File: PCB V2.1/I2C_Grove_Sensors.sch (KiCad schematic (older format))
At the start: 0 parts

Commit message: SunLeaf Alpha 0.2 and KiCAD Port
SunLeaf rev 2 called Alhpa 0.2 or 0.2a is the main component of this
commit. The entire hardware project has been ported to KiCAD libaries
and all. 0.2a features a revised formfactor, better ESP module, and many
fixes over the original. This version will also be capable of OTA
updates.
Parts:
- added C27, C28, C29, C30, C31: CL05B104JP5NNNC, PCB_Footprints:C0402, symbol CL05B104JP5NNNC
- added D6, D7, D8, D9: PESD3V3L2BT,215, PCB_Footprints:BAT20JFILM, symbol PESD3V3L2BT,215
- added J10, J11, J12, J9: S4B-PH-SM4-TB(LF)(SN), PCB_Footprints:S4B-PH-SM4-TB(LF)(SN), symbol S4B-PH-SM4-TB(LF)(SN)
- added R27, R28, R29, R30, R31, R32, R33, R34: RC1005F472CS, PCB_Footprints:R0402, symbol RC1005F472CS
- added U5: PCA9518DBQR, PCB_Footprints:PCA9518DBQR, symbol PCA9518DBQR
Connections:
- net labels added: +3.3V, GND
- wire segments 0 -> 46
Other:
- note added: "I2C Grove Sensors"

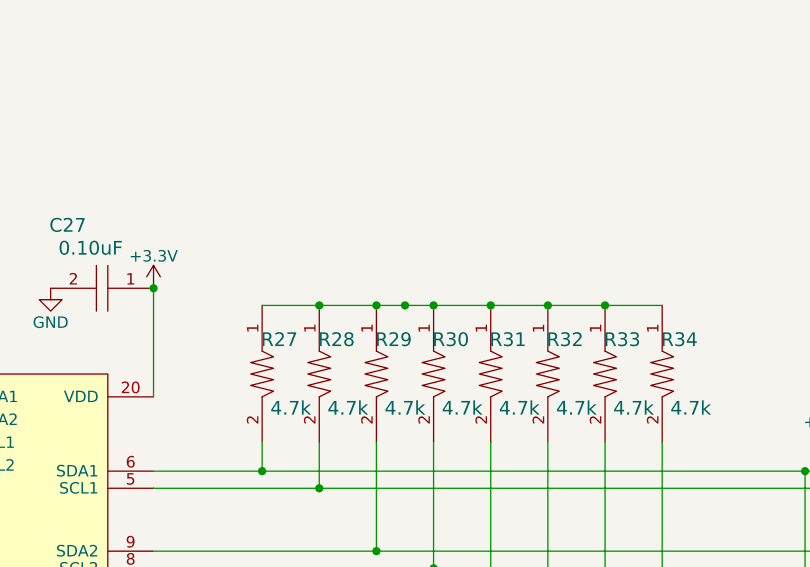
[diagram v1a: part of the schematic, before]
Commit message: Update
Updating KiCAD to the latest to get rounded corner pad support, filing
this commit as a backup of the project before update.
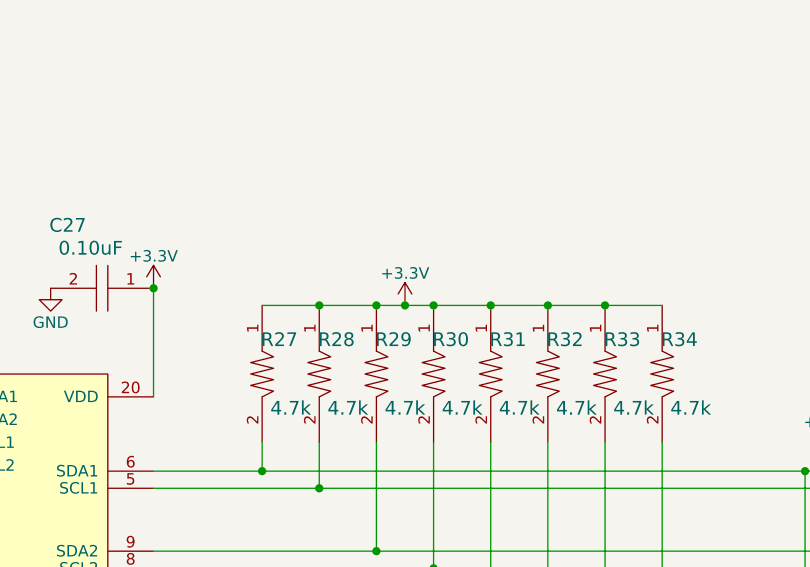
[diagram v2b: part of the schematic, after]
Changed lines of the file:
@@
 $EndComp
 $Comp
-L +3.3V #PWR053
+L +3.3V #PWR55
 U 1 1 57D9F38F
 P 2425 3000
-F 0 "#PWR053" H 2425 2850 50  0001 C CNN
+F 0 "#PWR55" H 2425 2850 50  0001 C CNN
 F 1 "+3.3V" H 2425 3140 50  0000 C CNN
 F 2 "" H 2425 3000 50  0000 C CNN
@@
 $EndComp
 $Comp
-L +3.3V #PWR054
+L +3.3V #PWR57
 U 1 1 57D9F6CC
 P 5375 3725
-F 0 "#PWR054" H 5375 3575 50  0001 C CNN
+F 0 "#PWR57" H 5375 3575 50  0001 C CNN
 F 1 "+3.3V" H 5375 3865 50  0000 C CNN
 F 2 "" H 5375 3725 50  0000 C CNN
@@
 $EndComp
 $Comp
-L +3.3V #PWR055
+L +3.3V #PWR62
 U 1 1 57D9F95C
 P 6950 4075
-F 0 "#PWR055" H 6950 3925 50  0001 C CNN
+F 0 "#PWR62" H 6950 3925 50  0001 C CNN
 F 1 "+3.3V" H 6950 4215 50  0000 C CNN
 F 2 "" H 6950 4075 50  0000 C CNN
@@
 $EndComp
 $Comp
-L +3.3V #PWR056
+L +3.3V #PWR68
 U 1 1 57DA0083
 P 10000 4775
-F 0 "#PWR056" H 10000 4625 50  0001 C CNN
+F 0 "#PWR68" H 10000 4625 50  0001 C CNN
 F 1 "+3.3V" H 10000 4915 50  0000 C CNN
 F 2 "" H 10000 4775 50  0000 C CNN
@@
 $EndComp
 $Comp
-L +3.3V #PWR057
+L +3.3V #PWR64
 U 1 1 57DA0445
 P 8400 4425
-F 0 "#PWR057" H 8400 4275 50  0001 C CNN
+F 0 "#PWR64" H 8400 4275 50  0001 C CNN
 F 1 "+3.3V" H 8400 4565 50  0000 C CNN
 F 2 "" H 8400 4425 50  0000 C CNN
@@
 $EndComp
 $Comp
-L GND #PWR058
+L GND #PWR59
 U 1 1 57DA07EC
 P 6000 3400
-F 0 "#PWR058" H 6000 3150 50  0001 C CNN
+F 0 "#PWR59" H 6000 3150 50  0001 C CNN
 F 1 "GND" H 6000 3250 50  0000 C CNN
 F 2 "" H 6000 3400 50  0000 C CNN
@@
 $EndComp
 $Comp
-L GND #PWR059
+L GND #PWR63
 U 1 1 57DA0A47
 P 7550 3750
-F 0 "#PWR059" H 7550 3500 50  0001 C CNN
+F 0 "#PWR63" H 7550 3500 50  0001 C CNN
 F 1 "GND" H 7550 3600 50  0000 C CNN
 F 2 "" H 7550 3750 50  0000 C CNN
@@
 $EndComp
 $Comp
-L GND #PWR060
+L GND #PWR65
 U 1 1 57DA0B33
 P 9100 4100
-F 0 "#PWR060" H 9100 3850 50  0001 C CNN
+F 0 "#PWR65" H 9100 3850 50  0001 C CNN
 F 1 "GND" H 9100 3950 50  0000 C CNN
 F 2 "" H 9100 4100 50  0000 C CNN
@@
 $EndComp
 $Comp
-L GND #PWR061
+L GND #PWR69
 U 1 1 57DA0DF0
 P 10675 4450
-F 0 "#PWR061" H 10675 4200 50  0001 C CNN
+F 0 "#PWR69" H 10675 4200 50  0001 C CNN
 F 1 "GND" H 10675 4300 50  0000 C CNN
 F 2 "" H 10675 4450 50  0000 C CNN
@@
 $EndComp
 $Comp
-L GND #PWR062
+L GND #PWR67
 U 1 1 57DA24B2
 P 9425 6000
-F 0 "#PWR062" H 9425 5750 50  0001 C CNN
+F 0 "#PWR67" H 9425 5750 50  0001 C CNN
 F 1 "GND" H 9425 5850 50  0000 C CNN
 F 2 "" H 9425 6000 50  0000 C CNN
@@
 $EndComp
 $Comp
-L +3.3V #PWR063
+L +3.3V #PWR66
 U 1 1 57DA24F6
 P 9425 5550
-F 0 "#PWR063" H 9425 5400 50  0001 C CNN
+F 0 "#PWR66" H 9425 5400 50  0001 C CNN
 F 1 "+3.3V" H 9425 5690 50  0000 C CNN
 F 2 "" H 9425 5550 50  0000 C CNN
@@
 Connection ~ 7000 4925
 $Comp
-L GND #PWR064
+L GND #PWR54
 U 1 1 57DA31E3
 P 1975 3000
-F 0 "#PWR064" H 1975 2750 50  0001 C CNN
+F 0 "#PWR54" H 1975 2750 50  0001 C CNN
 F 1 "GND" H 1975 2850 50  0000 C CNN
 F 2 "" H 1975 3000 50  0000 C CNN
@@
 $EndComp
 $Comp
-L GND #PWR065
+L GND #PWR58
 U 1 1 57DA32E0
 P 5875 5725
-F 0 "#PWR065" H 5875 5475 50  0001 C CNN
+F 0 "#PWR58" H 5875 5475 50  0001 C CNN
 F 1 "GND" H 5875 5575 50  0000 C CNN
 F 2 "" H 5875 5725 50  0000 C CNN
@@
 $EndComp
 $Comp
-L GND #PWR066
+L GND #PWR60
 U 1 1 57DA332D
 P 6400 5725
-F 0 "#PWR066" H 6400 5475 50  0001 C CNN
+F 0 "#PWR60" H 6400 5475 50  0001 C CNN
 F 1 "GND" H 6400 5575 50  0000 C CNN
 F 2 "" H 6400 5725 50  0000 C CNN
@@
 $EndComp
 $Comp
-L GND #PWR067
+L GND #PWR61
 U 1 1 57DA337A
 P 6925 5725
-F 0 "#PWR067" H 6925 5475 50  0001 C CNN
+F 0 "#PWR61" H 6925 5475 50  0001 C CNN
 F 1 "GND" H 6925 5575 50  0000 C CNN
 F 2 "" H 6925 5725 50  0000 C CNN
@@
 	1275 4425 1000 4425
 $Comp
-L GND #PWR068
+L GND #PWR53
 U 1 1 57DA52FC
 P 1275 4925
-F 0 "#PWR068" H 1275 4675 50  0001 C CNN
+F 0 "#PWR53" H 1275 4675 50  0001 C CNN
 F 1 "GND" H 1275 4775 50  0000 C CNN
 F 2 "" H 1275 4925 50  0000 C CNN
@@
 Text Notes 4275 1575 0    197  ~ 39
 I2C Grove Sensors
+$Comp
+L +3.3V #PWR56
+U 1 1 57DB6494
+P 3525 3075
+F 0 "#PWR56" H 3525 2925 50  0001 C CNN
+F 1 "+3.3V" H 3525 3215 50  0000 C CNN
+F 2 "" H 3525 3075 50  0000 C CNN
+F 3 "" H 3525 3075 50  0000 C CNN
+	1    3525 3075
+	1    0    0    -1
+$EndComp
 $EndSCHEMATC

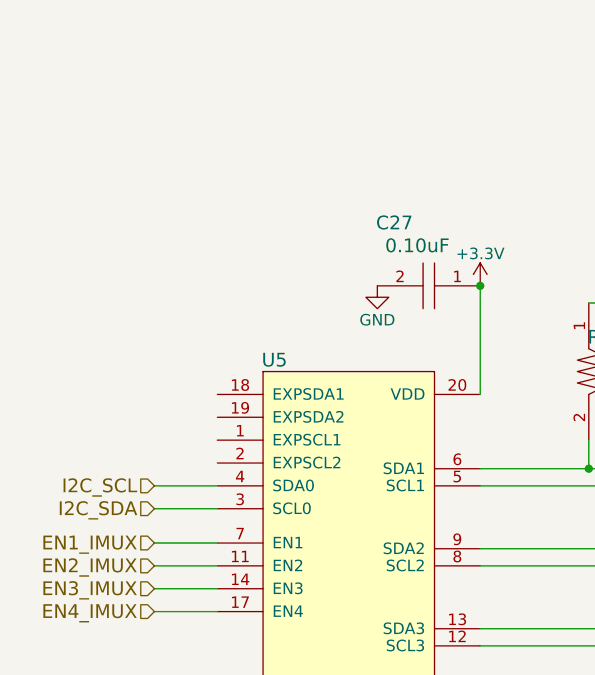
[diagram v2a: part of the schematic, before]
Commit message: Placement
Heavy progress on component placement in KiCAD for SunLEaf V2,
committing to save progress, nightly builds of KiCAD are very crash
prone.
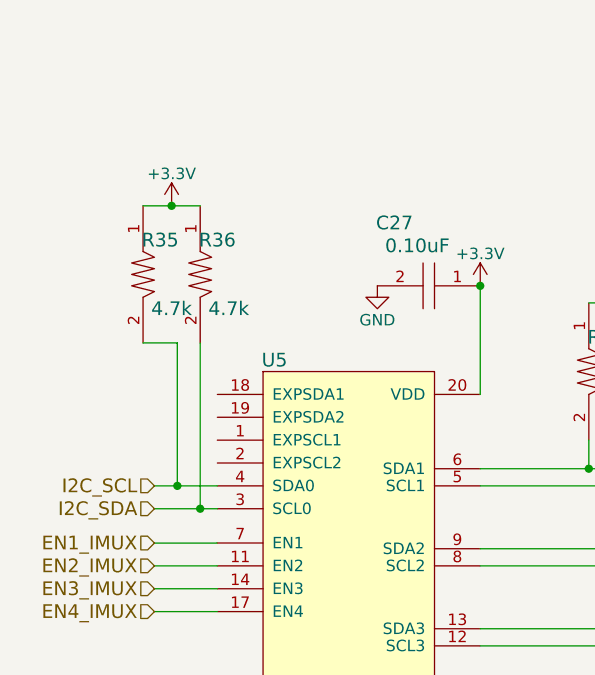
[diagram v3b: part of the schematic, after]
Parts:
- added R35, R36: RC1005F472CS, PCB_Footprints:R0402, symbol RC1005F472CS
- D6, D7, D8, D9: footprint PCB_Footprints:BAT20JFILM -> PCB_Footprints:PESD3V3L2BT,215
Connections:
- wire segments 46 -> 50

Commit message: Placement progress
Placement is 99% done board is being resized. Next commit TVS diode
pairs will be fliped and the baord further resized.
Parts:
- removed C28, C29, C30, C31: CL05B104JP5NNNC, PCB_Footprints:C0402, symbol CL05B104JP5NNNC
- removed J10, J11, J12, J9: S4B-PH-SM4-TB(LF)(SN), PCB_Footprints:S4B-PH-SM4-TB(LF)(SN), symbol S4B-PH-SM4-TB(LF)(SN)
- added J10, J11, J12, J9: B4B-PH-K-S(LF)(SN), PCB_Footprints:B4B-PH-K-S(LF)(SN), symbol B4B-PH-K-S(LF)(SN)
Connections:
- wire segments 50 -> 48

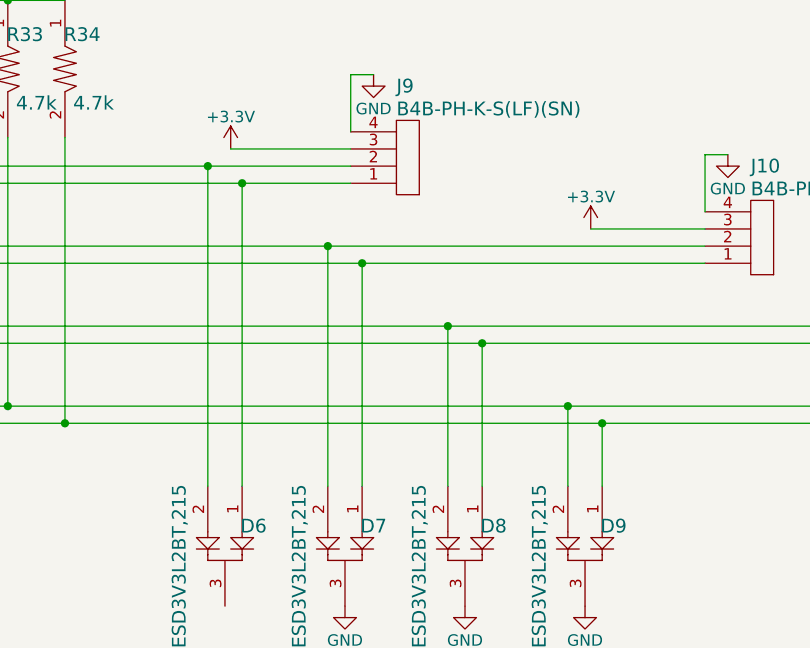
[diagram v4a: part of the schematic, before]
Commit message: Internal Planes
Internal Planes added, small amount of routing left.
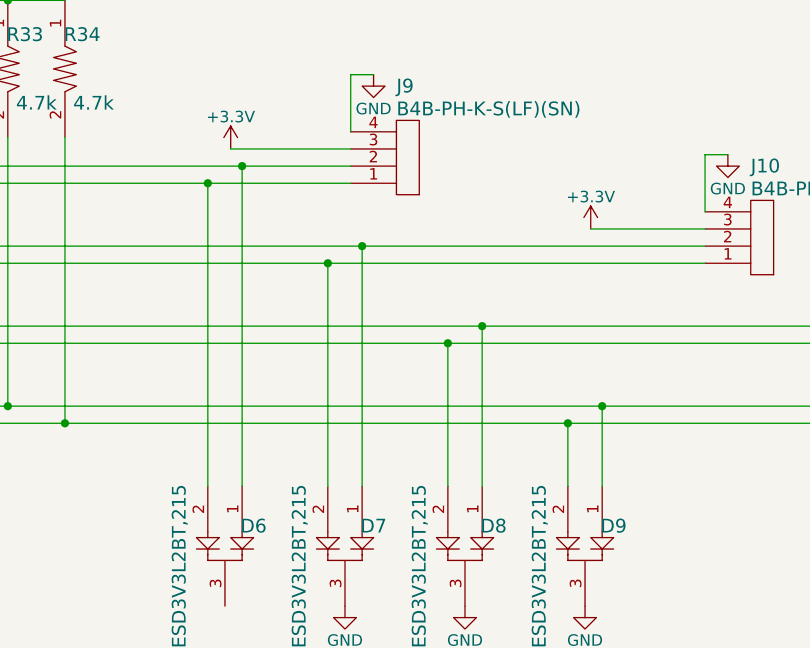
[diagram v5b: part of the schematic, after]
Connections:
- net at J9.1, R28.2, U5.5 (SCL1): now also D6.2; no longer D6.1
- net at J9.2, R27.2, U5.6 (SDA1): now also D6.1; no longer D6.2
- net at J11.1, R32.2, U5.12 (SCL3): now also D8.2; no longer D8.1
- net at J11.2, R31.2, U5.13 (SDA3): now also D8.1; no longer D8.2
- net at J12.1, R34.2, U5.15 (SCL4): now also D9.2; no longer D9.1
- net at J12.2, R33.2, U5.16 (SDA4): now also D9.1; no longer D9.2
- net at J10.1, R30.2, U5.8 (SCL2): now also D7.2; no longer D7.1
- net at J10.2, R29.2, U5.9 (SDA2): now also D7.1; no longer D7.2
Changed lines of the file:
@@
 LIBS:contrib
 LIBS:valves
-LIBS:stm32
-LIBS:ESP8266
 LIBS:HydroPWNics_Lib
 LIBS:ESP32-footprints-Shem-Lib
@@
 Wire Wire Line
 	5900 3400 6000 3400
-Wire Wire Line
-	5275 5200 5275 3800
-Connection ~ 5275 3800
-Wire Wire Line
-	5425 5200 5425 3875
-Connection ~ 5425 3875
-Wire Wire Line
-	5800 5200 5800 4150
-Connection ~ 5800 4150
-Wire Wire Line
-	5950 5200 5950 4225
-Connection ~ 5950 4225
-Wire Wire Line
-	6325 5200 6325 4500
-Connection ~ 6325 4500
-Wire Wire Line
-	6475 5200 6475 4575
-Connection ~ 6475 4575
-Wire Wire Line
-	6850 5200 6850 4850
-Connection ~ 6850 4850
-Wire Wire Line
-	7000 5200 7000 4925
-Connection ~ 7000 4925
+Connection ~ 5425 3800
+Connection ~ 5275 3875
+Connection ~ 5950 4150
+Connection ~ 5800 4225
+Connection ~ 6475 4500
+Connection ~ 6325 4575
+Connection ~ 7000 4850
+Connection ~ 6850 4925
 $Comp
 L GND #PWR57
@@
 	-1   0    0    1
 $EndComp
+Wire Wire Line
+	5275 3875 5275 5200
+Wire Wire Line
+	5425 5200 5425 3800
+Wire Wire Line
+	5950 4150 5950 5200
+Wire Wire Line
+	5800 4225 5800 5200
+Wire Wire Line
+	6475 4500 6475 5200
+Wire Wire Line
+	6325 5200 6325 4575
+Wire Wire Line
+	6850 4925 6850 5200
+Wire Wire Line
+	7000 5200 7000 4850
 $EndSCHEMATC
